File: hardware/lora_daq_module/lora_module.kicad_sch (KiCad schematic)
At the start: 22 parts, among them J1 SMA_Edge_50Ω, J2 USB_C_Receptacle_USB2.0_14P, SW1 SW_Push, U2 CAT24C256, U3 CP2102N-Axx-xQFN20, U4 Wio-E5_STM32WLE5JC

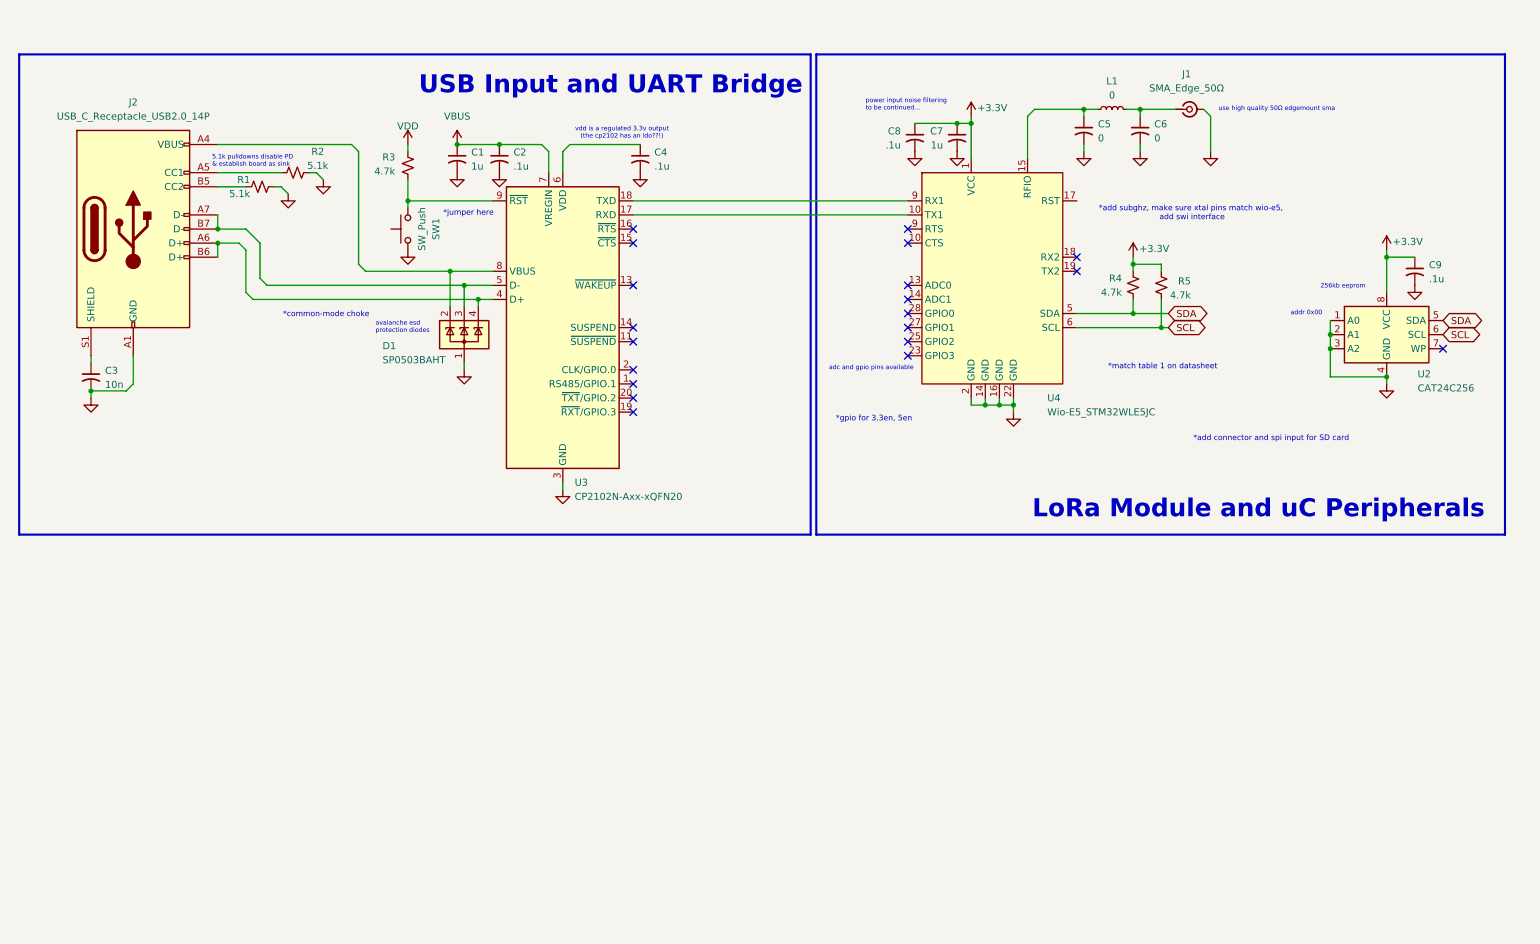
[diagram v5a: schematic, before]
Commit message: add sd card, swd connector, external uart, and update pinout for wio-e5
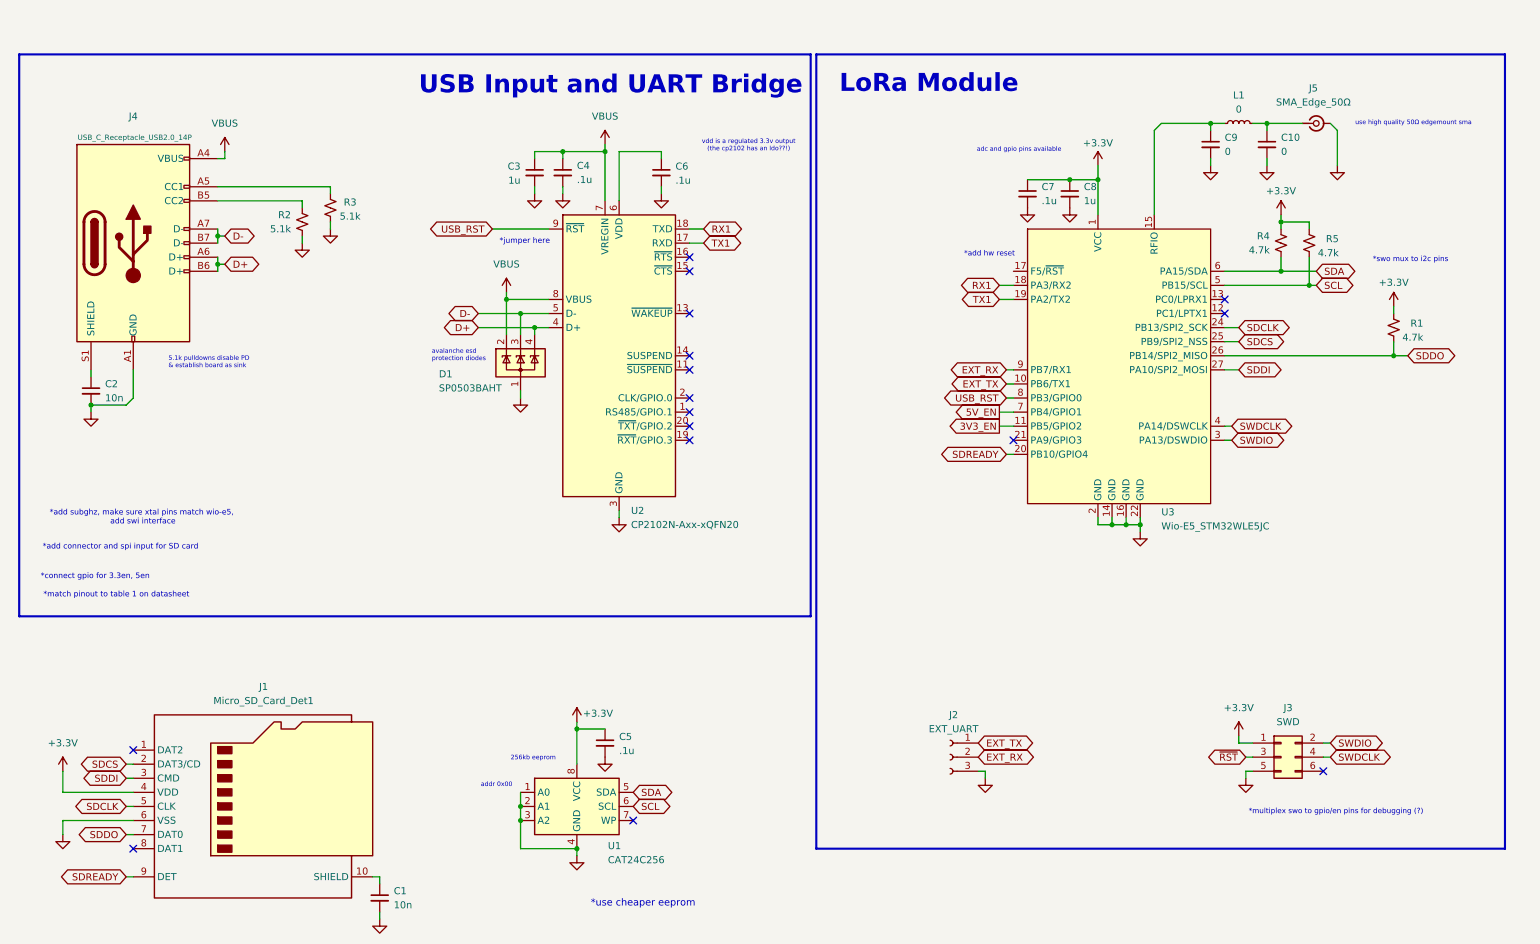
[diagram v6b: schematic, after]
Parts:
- removed R3: 4.7k, symbol Device:R_Small_US
- removed SW1: SW_Push, symbol Switch:SW_Push
- added C1: 10n, symbol Device:C_Small
- added J1: Micro_SD_Card_Det1, symbol Connector:Micro_SD_Card_Det1
- added J2: EXT_UART, symbol Connector:Conn_01x03_Socket
- added J3: SWD, symbol Connector_Generic:Conn_02x03_Odd_Even
- added R1: 4.7k, symbol Device:R_Small_US
- C10: renamed from C6; symbol Device:C_Small_US -> Device:C_Small
- C2: renamed from C3; symbol Device:C_Small_US -> Device:C_Small
- C3: renamed from C1; symbol Device:C_Small_US -> Device:C_Small
- C4: renamed from C2; symbol Device:C_Small_US -> Device:C_Small
- C5: renamed from C9; symbol Device:C_Small_US -> Device:C_Small
- C6: renamed from C4; symbol Device:C_Small_US -> Device:C_Small
- C7: renamed from C8; symbol Device:C_Small_US -> Device:C_Small
- C8: renamed from C7; symbol Device:C_Small_US -> Device:C_Small
- C9: renamed from C5; symbol Device:C_Small_US -> Device:C_Small
- renumbered J2 to J4, J1 to J5, R1 to R2, R2 to R3, U2 to U1, U3 to U2, U4 to U3
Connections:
- net +3.3V: now also J1.4 (VDD), J3.1 (Pin_1), R1.2
- net GND: now also R2.1, R3.1, C1.2, J1.6 (VSS), J2.3 (Pin_3), J3.5 (Pin_5); no longer R2.2, R3.2
- net SCL: now also U3.5 (PB15/SCL); no longer U3.6 (SCL)
- net SDA: now also U3.6 (PA15/SDA); no longer U3.5 (SDA)
- net VBUS: now also D1.2 (K), J4.A4 (VBUS), J4.A9 (VBUS), J4.B4 (VBUS), J4.B9 (VBUS), U2.8 (VBUS)
- net at J4.A5 (CC1): now also R3.2; no longer R3.1
- net D+: now reaches D1.4 (K), J4.A6 (D+), J4.B6 (D+), U2.4 (D+)
- net D-: now reaches D1.3 (K), J4.A7 (D-), J4.B7 (D-), U2.5 (D-)
- net at J4.B5 (CC2): now also R2.2; no longer R2.1
- net EXT_TX: now reaches U3.10 (PB6/TX1)
- net EXT_TX: now also J2.1 (Pin_1)
- net TX1: now reaches U2.17 (RXD)
- net TX1: now also U3.19 (PA2/TX2); no longer U3.10 (CTS)
- net RX1: now reaches U3.18 (PA3/RX2)
- net RX1: now also U2.18 (TXD)
- net SDCS: now reaches U3.25 (PB9/SPI2_NSS)
- net SDCS: now also J1.2 (DAT3/CD)
- net SDDI: now reaches U3.27 (PA10/SPI2_MOSI)
- net SDDI: now also J1.3 (CMD)
- net EXT_RX: now reaches U3.9 (PB7/RX1)
- net EXT_RX: now also J2.2 (Pin_2)
- net USB_RST: now reaches U2.9 (~{RST})
- net USB_RST: now also U3.8 (PB3/GPIO0)
- new net: C1.1, J1.10 (SHIELD)
- new net 3V3_EN: U3.11 (PB5/GPIO2)
- new net 5V_EN: U3.7 (PB4/GPIO1)
- new net SDCLK: J1.5 (CLK), U3.24 (PB13/SPI2_SCK)
- new net SDDO: J1.7 (DAT0), R1.1, U3.26 (PB14/SPI2_MISO)
- new net SDREADY: J1.9 (DET), U3.20 (PB10/GPIO4)
- new net SWDCLK: J3.4 (Pin_4), U3.4 (PA14/DSWCLK)
- new net SWDIO: J3.2 (Pin_2), U3.3 (PA13/DSWDIO)
- new net ~{RST}: J3.3 (Pin_3)
- no-connect marks 20 -> 16
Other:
- note added: "*add hw reset"
- note added: "*connect gpio for 3.3en, 5en"
- note added: "*match pinout to table 1 on datasheet"
- note added: "*multiplex swo to gpio/en pins for debugging (?)"
- note added: "*swo mux to i2c pins"
- note added: "*use cheaper eeprom"
- note added: "LoRa Module"
- note removed: "*common-mode choke"
- note removed: "*gpio for 3.3en, 5en"
- note removed: "*match table 1 on datasheet"
- note removed: "LoRa Module and uC Peripherals"
- note removed: "power input noise filtering to be continued..."
- moved on the sheet: C10, C2, C3, C4, C5, C6, C7, C8, C9, D1, J4, J5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

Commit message: updated power schematic to include power switching IC for battery/usb power, minor changes to lora module schematic, added footprints to all component and began with the preliminary layout based on data sheet and application note reccomendations for each component.
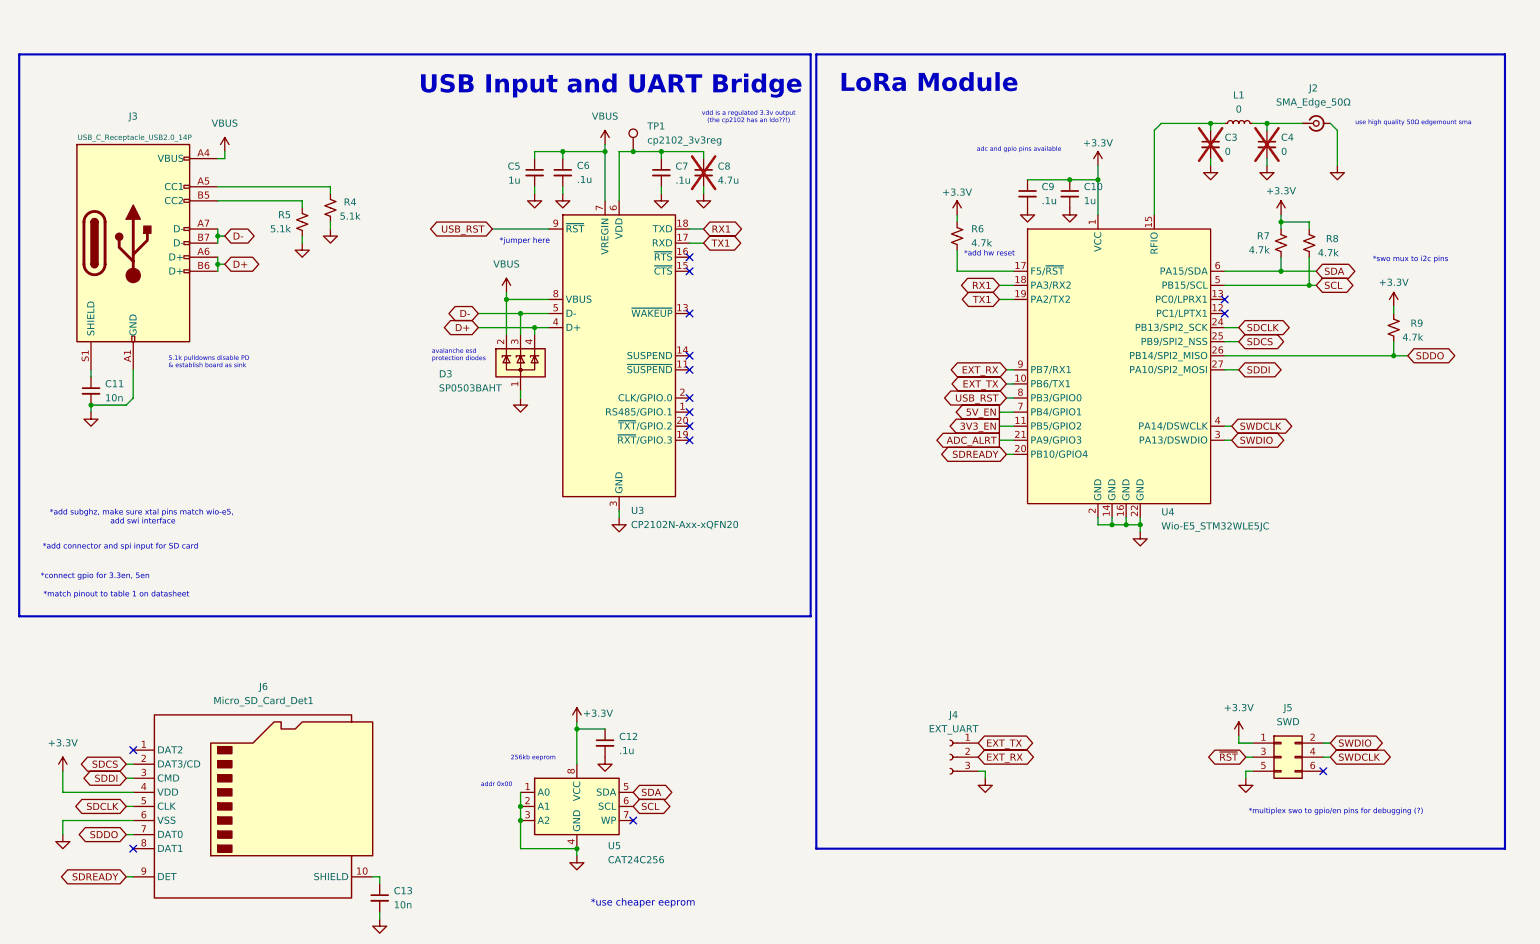
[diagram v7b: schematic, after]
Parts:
- added C8: 4.7u, Capacitor_SMD:C_1206_3216Metric, symbol Device:C_Small
- added R6: 4.7k, Resistor_SMD:R_0603_1608Metric, symbol Device:R_Small_US
- added TP1: cp2102_3v3reg, TestPoint:TestPoint_Pad_3.0x3.0mm, symbol Connector:TestPoint
- C10: renamed from C8; footprint (none) -> Capacitor_SMD:C_0603_1608Metric
- C11: renamed from C2; footprint (none) -> Capacitor_SMD:C_0603_1608Metric
- C12: renamed from C5; footprint (none) -> Capacitor_SMD:C_0603_1608Metric
- C13: renamed from C1; footprint (none) -> Capacitor_SMD:C_0603_1608Metric
- C3: renamed from C9; footprint (none) -> Capacitor_SMD:C_0603_1608Metric; now not fitted
- C4: renamed from C10; footprint (none) -> Capacitor_SMD:C_0603_1608Metric; now not fitted
- C5: renamed from C3; footprint (none) -> Capacitor_SMD:C_0603_1608Metric
- C6: renamed from C4; footprint (none) -> Capacitor_SMD:C_0603_1608Metric
- C7: renamed from C6; footprint (none) -> Capacitor_SMD:C_0603_1608Metric
- C9: renamed from C7; footprint (none) -> Capacitor_SMD:C_0603_1608Metric
- J2: renamed from J5; footprint (none) -> Connector_Coaxial:SMA_Molex_73251-1153_EdgeMount_Horizontal
- J3: renamed from J4; footprint (none) -> Connector_USB:USB_C_Receptacle_Molex_105450-0101
- J4: renamed from J2; footprint (none) -> Connector_JST:JST_EH_B3B-EH-A_1x03_P2.50mm_Vertical
- J5: renamed from J3; footprint (none) -> Connector_PinHeader_2.54mm:PinHeader_2x03_P2.54mm_Vertical
- J6: renamed from J1; footprint (none) -> Connector_Card:microSD_HC_Molex_104031-0811
- L1: footprint (none) -> Resistor_SMD:R_0603_1608Metric
- R4: renamed from R3; footprint (none) -> Resistor_SMD:R_0603_1608Metric
- R5: renamed from R2; footprint (none) -> Resistor_SMD:R_0603_1608Metric
- R7: renamed from R4; footprint (none) -> Resistor_SMD:R_0603_1608Metric
- R8: renamed from R5; footprint (none) -> Resistor_SMD:R_0603_1608Metric
- R9: renamed from R1; footprint (none) -> Resistor_SMD:R_0603_1608Metric
- U3: renamed from U2; footprint Package_DFN_QFN:SiliconLabs_QFN-20-1EP_3x3mm_P0.5mm -> Package_DFN_QFN:SiliconLabs_QFN-20-1EP_3x3mm_P0.5mm_EP1.8x1.8mm
- U4: renamed from U3; footprint (none) -> LoRa-E5:LoRa-E5
- U5: renamed from U1; footprint (none) -> Package_SO:SOIC-8-1EP_3.9x4.9mm_P1.27mm_EP2.29x3mm
- renumbered D1 to D3
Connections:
- net +3.3V: now also R6.1
- net GND: now also C8.2
- net at U4.17 (F5/~{RST}): now also R6.2
- net ADC_ALRT: now reaches U4.21 (PA9/GPIO3)
- net at C7.1, U3.6 (VDD): now also C8.1, TP1.1
- no-connect marks 16 -> 15
